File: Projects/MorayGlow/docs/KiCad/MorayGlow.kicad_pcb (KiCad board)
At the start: 2 copper layers, 25 parts, among them J1 Conn_01x04, J2 RGB LED, J5 Barrel Jack, Q1 IRFML8244, Q2 IRFML8244, Q3 IRFML8244, SW1 SW_DIP_x01, U1 XIAO-ESP32-S3-Plus-SMD, U3 LM2596S-5

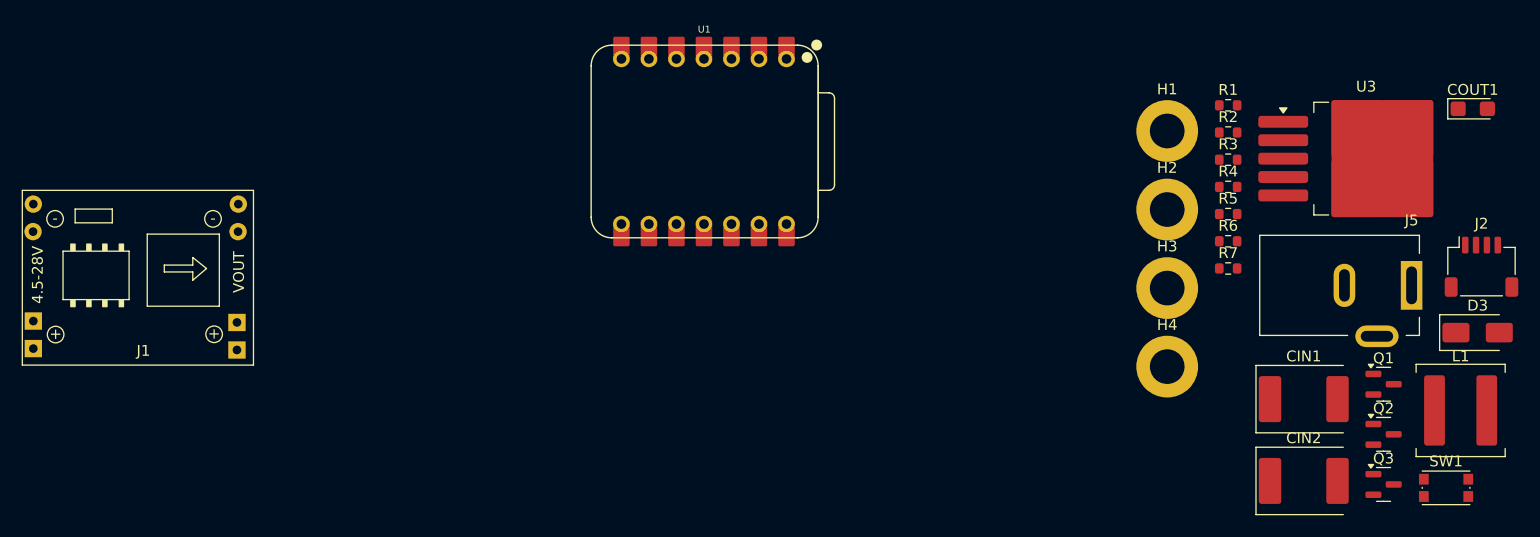
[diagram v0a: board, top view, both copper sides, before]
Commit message: updated schmatic and pcb
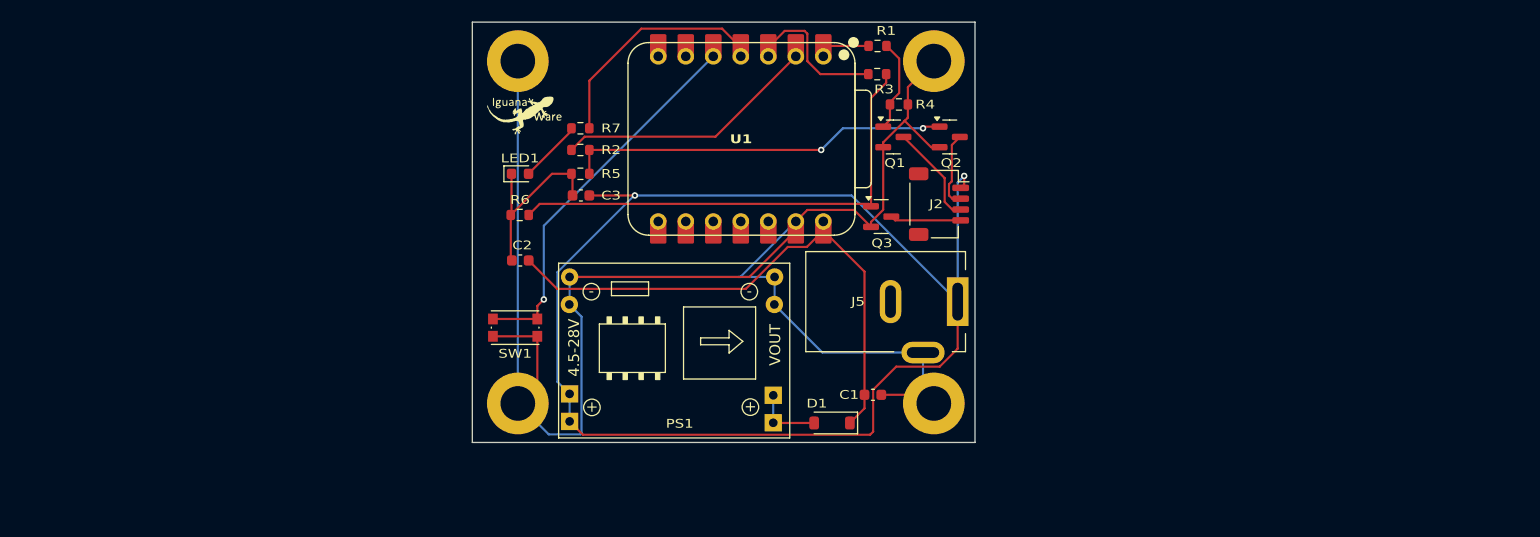
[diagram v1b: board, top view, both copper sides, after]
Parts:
- removed CIN1, CIN2: 330uF, Capacitor_Tantalum_SMD:CP_EIA-7360-38_Kemet-E
- removed COUT1: 220uF, Capacitor_Tantalum_SMD:CP_EIA-3216-18_Kemet-A
- removed D3: SK32, Diode_SMD:D_SMA
- removed J1: Conn_01x04, MP1584EN:SRT_MPT1584EN_Module
- removed L1: 3uH, Inductor_SMD:L_Coilcraft_XAL7070-XXX
- removed U3: LM2596S-5, Package_TO_SOT_SMD:TO-263-5_TabPin3
- added C1: 0.1uF, Capacitor_SMD:C_0603_1608Metric, F.Cu at (179.0, 121.8)
- added C2: 10uF, Capacitor_SMD:C_0603_1608Metric, F.Cu at (146.4, 109.4)
- added C3: 0.1uF, Capacitor_SMD:C_0603_1608Metric, F.Cu at (152.0, 103.4)
- added D1: 1N5819HW-7-F, Diode_SMD:D_SOD-123, F.Cu at (175.2, 124.4)
- added G***: LOGO, LOGO, F.Cu at (146.8, 96.0)
- added G***: LOGO, LOGO, B.Cu at (160.2, 97.8)
- added LED1: LED, LED_SMD:LED_0603_1608Metric, F.Cu at (146.4, 101.4)
- added PS1: MP1584 5V buck module, MP1584EN:SRT_MPT1584EN_Module, F.Cu at (161.1, 117.1)
- Q1, Q2, Q3: value IRFML8244 -> IRLML6344TRPBF
- moved SW1 87.2 mm to (145.9, 115.6)
- moved R6 65.4 mm to (146.4, 105.2), turned to 180 degrees
- moved R7 61.2 mm to (152.0, 97.2)
- moved H3 60.9 mm to (146.2, 122.6)
- moved H1 60.3 mm to (146.2, 91.0)
- moved R5 59.9 mm to (152.0, 101.4), turned to 180 degrees
- moved R2 59.8 mm to (152.0, 99.2), turned to 180 degrees
- moved Q3 52.6 mm to (179.7, 105.3)
- moved Q1 50.7 mm to (180.9, 98.0)
- moved J2 50.4 mm to (185.1, 104.2), turned to -90 degrees
- moved Q2 48.6 mm to (186.1, 98.0)
- moved J5 41.9 mm to (186.8, 113.2)
- moved R3 33.3 mm to (179.4, 92.2), turned to 180 degrees
- moved R1 32.8 mm to (179.4, 89.6), turned to 180 degrees
- moved R4 31.3 mm to (181.4, 95.0)
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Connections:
- Q1 pad 1: LED_R -> Net-(Q1-Pad1)
- Q1 pad 2: Net-(Q1-G) -> <NO NET>
- Q1 pad 3: Net-(Q1-S) -> LED_R
- Q2 pad 1: LED_G -> Net-(Q2-Pad1)
- Q2 pad 2: Net-(Q2-G) -> <NO NET>
- Q2 pad 3: Net-(Q2-S) -> LED_G
- Q3 pad 1: LED_B -> Net-(Q3-Pad1)
- Q3 pad 2: Net-(Q3-G) -> <NO NET>
- Q3 pad 3: Net-(Q3-S) -> LED_B
- R1 pad 1: Net-(Q1-G) -> Net-(Q1-Pad1)
- R2 pad 1: Net-(Q2-G) -> Net-(Q2-Pad1)
- R3 pad 1: Net-(Q3-G) -> Net-(Q3-Pad1)
- R4 pad 1: Net-(Q1-S) -> Net-(Q1-Pad1)
- R5 pad 1: Net-(Q2-S) -> Net-(Q2-Pad1)
- R6 pad 1: Net-(Q3-S) -> Net-(Q3-Pad1)
- R7 pad 1: unconnected-(R7-Pad1) -> Net-(LED1-A)
- SW1 pad 1: <NO NET> -> CMD_BTN
- SW1 pad 2: CMD_BTN -> <NO NET>
- U1 pad 14: VDD_5V -> Net-(D1-K)
- U1 pad 4: unconnected-(U1-GPIO4_A3_D3-Pad4) -> STATUS_LED
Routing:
- net <NO NET>: track 0.00 -> 189.5 mm
- net VCC_12V: track 0.00 -> 121.7 mm, vias 0 -> 2
- net Net-(D1-K): track 0.00 -> 50.4 mm
- net Net-(Q3-Pad1): track 0.00 -> 44.9 mm
- net Net-(Q2-Pad1): track 0.00 -> 35.4 mm, vias 0 -> 2
- net CMD_BTN: track 0.00 -> 35.1 mm, vias 0 -> 1
- net RGB_G: track 0.00 -> 24.3 mm
- net STATUS_LED: track 0.00 -> 21.1 mm
- net RGB_B: track 0.00 -> 13.0 mm
- net LED_R: track 0.00 -> 9.34 mm
- net Net-(Q1-Pad1): track 0.00 -> 8.55 mm
- net LED_G: track 0.00 -> 7.01 mm
- net LED_B: track 0.00 -> 6.54 mm
- net VDD_5V: track 0.00 -> 6.32 mm
- net Net-(LED1-A): track 0.00 -> 5.84 mm
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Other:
- board outline added: 46.4 x 38.8 mm
